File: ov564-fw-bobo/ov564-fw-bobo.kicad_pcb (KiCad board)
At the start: 2 copper layers, 50.8 x 22.9 mm, 6 parts

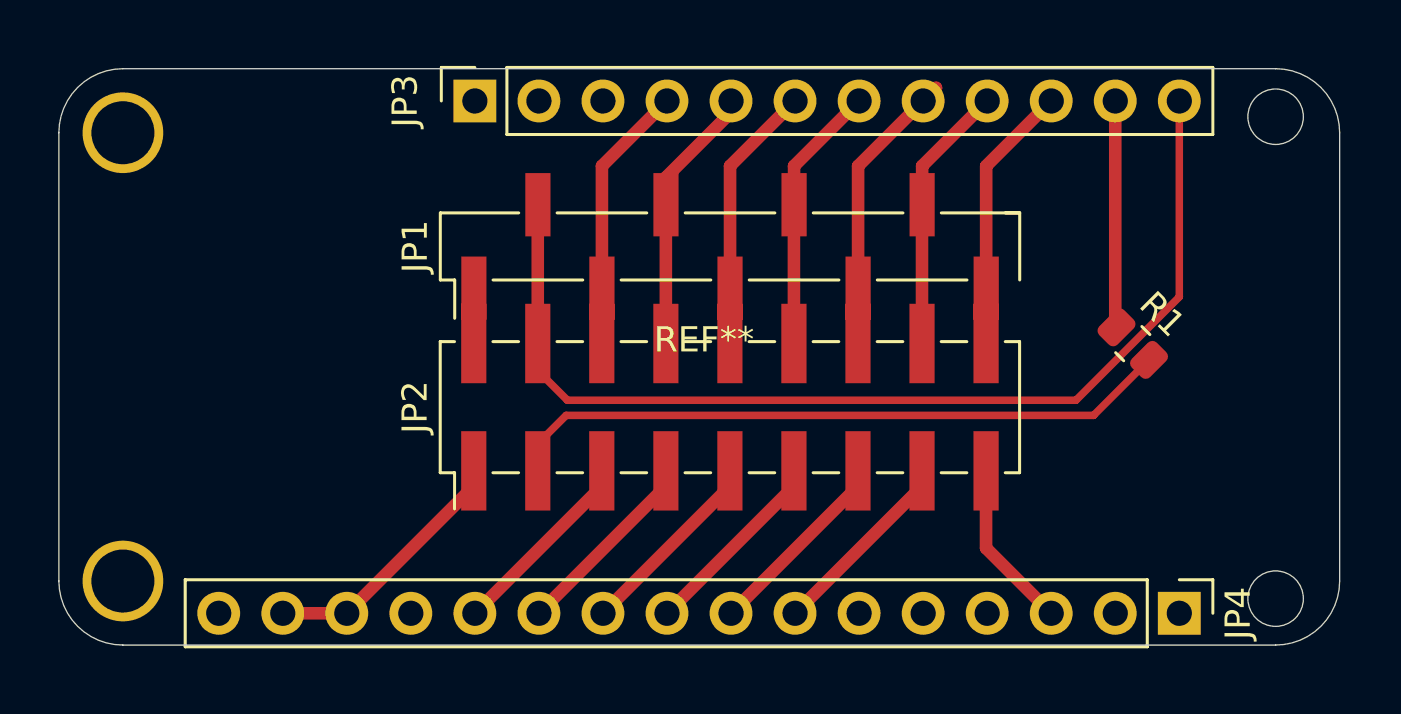
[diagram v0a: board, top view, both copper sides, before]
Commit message: increased FW size, added resistor jump
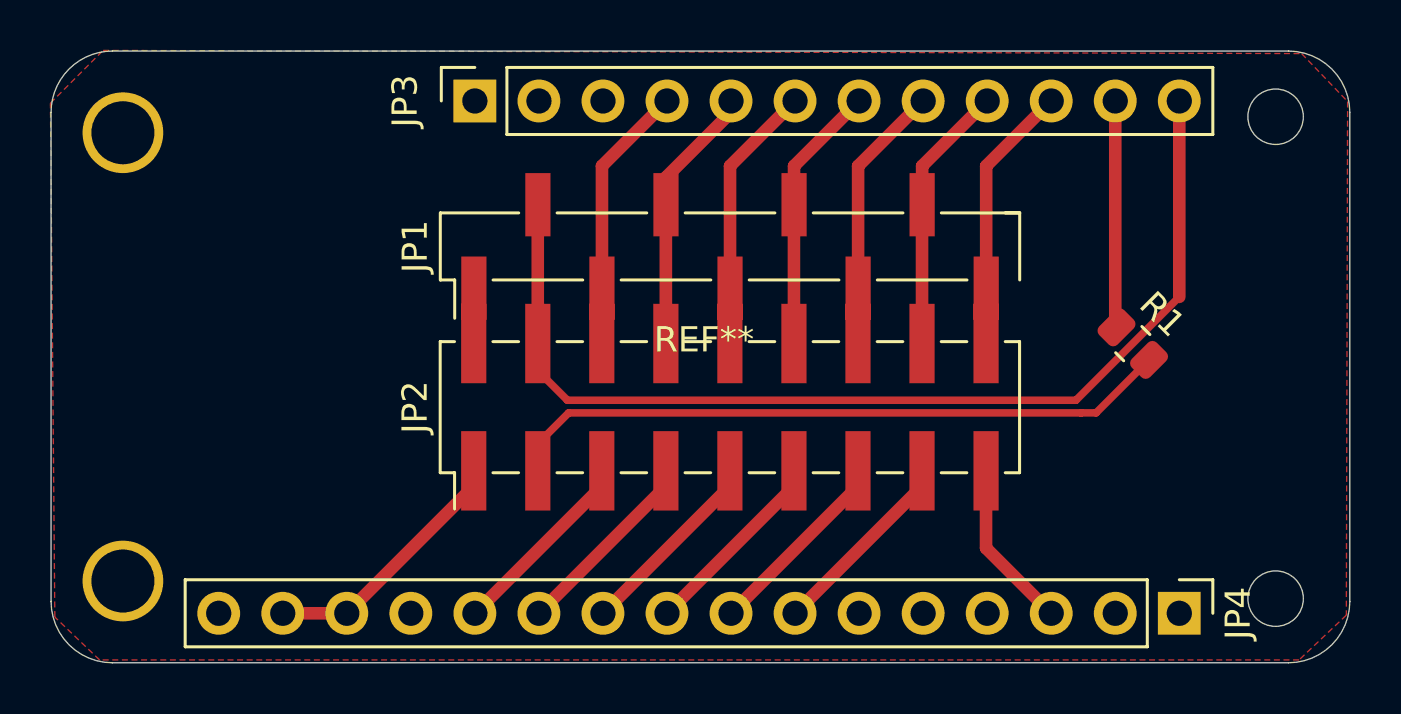
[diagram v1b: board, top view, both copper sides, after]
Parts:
- removed the REF** at (162.9, 92.8)
- added REF**: featherwing-empty, footprints:feeatherwing-esp32s3-blank, F.Cu at (162.9, 92.8)
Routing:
- net GND: track 2.20 -> 0.01 mm
- net /DATA4: track 11.4 -> 10.7 mm
- added copper zone on F.Cu, net GND
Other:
- board size 50.8 x 22.9 mm -> 51.5 x 24.3 mm
